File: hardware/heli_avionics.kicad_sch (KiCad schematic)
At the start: 40 parts, among them J1 UPDI, SW1 Reset, U1 ATmega4808-A, U2 nRF24L01P, U3 DRV8212, U4 DRV8212, U5 BMP390L, U6 TPS7A2030PDBV, Y1 16MHz

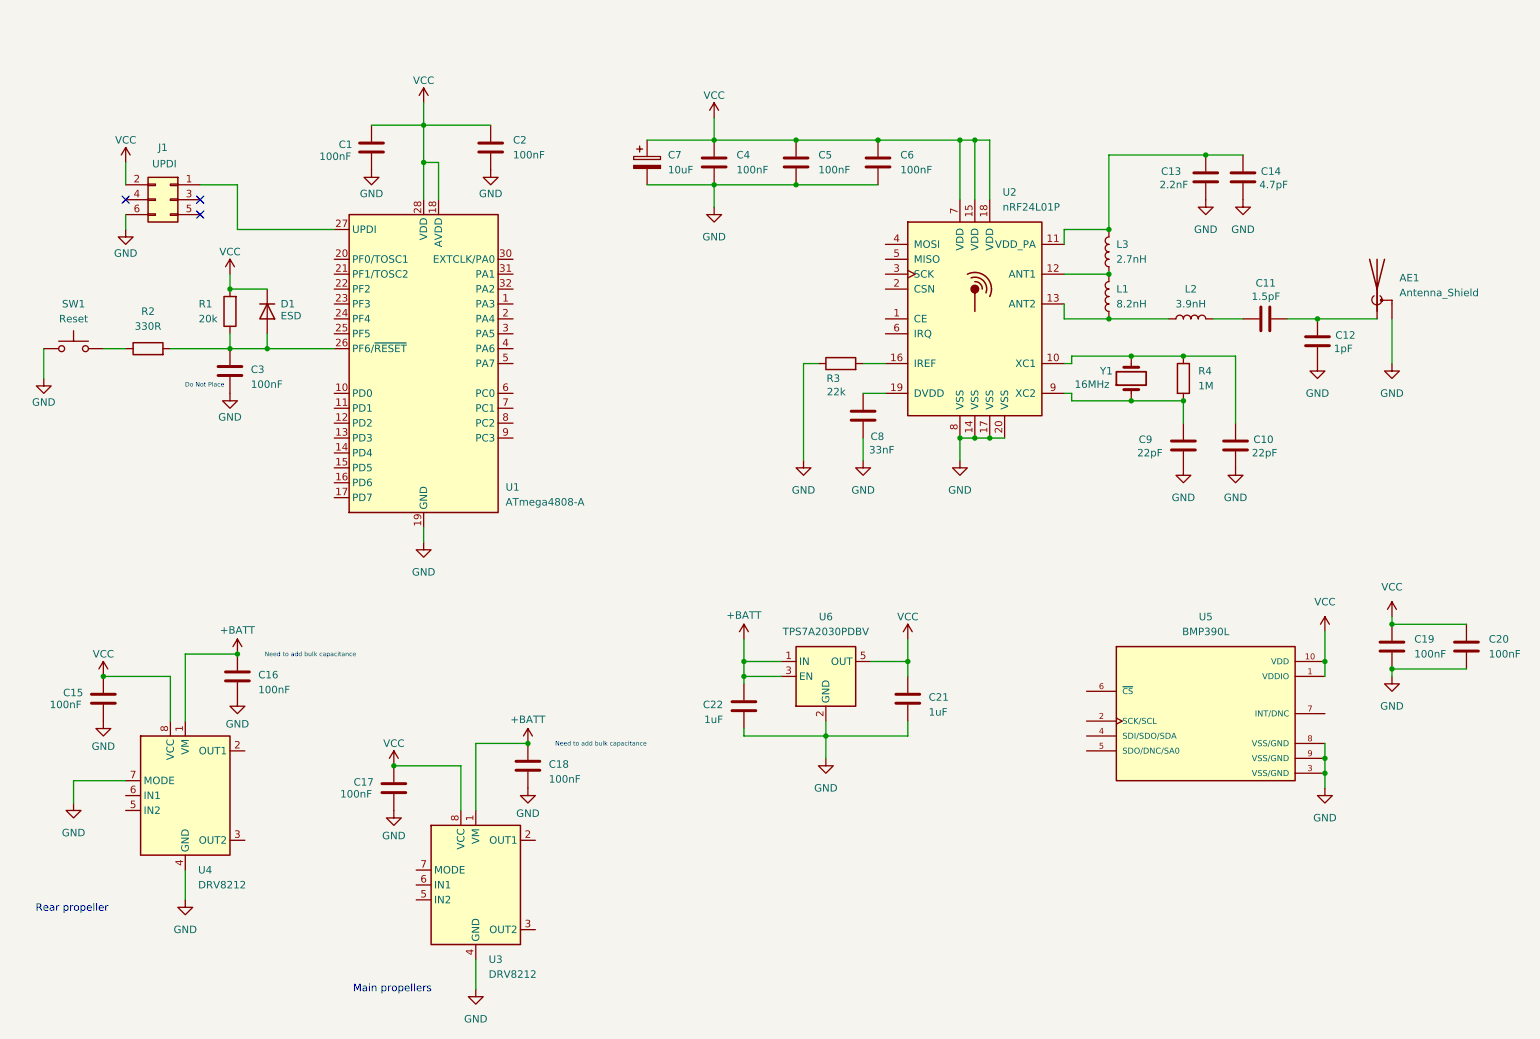
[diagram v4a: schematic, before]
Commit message: Finish motor driver circuits and move to subsheet
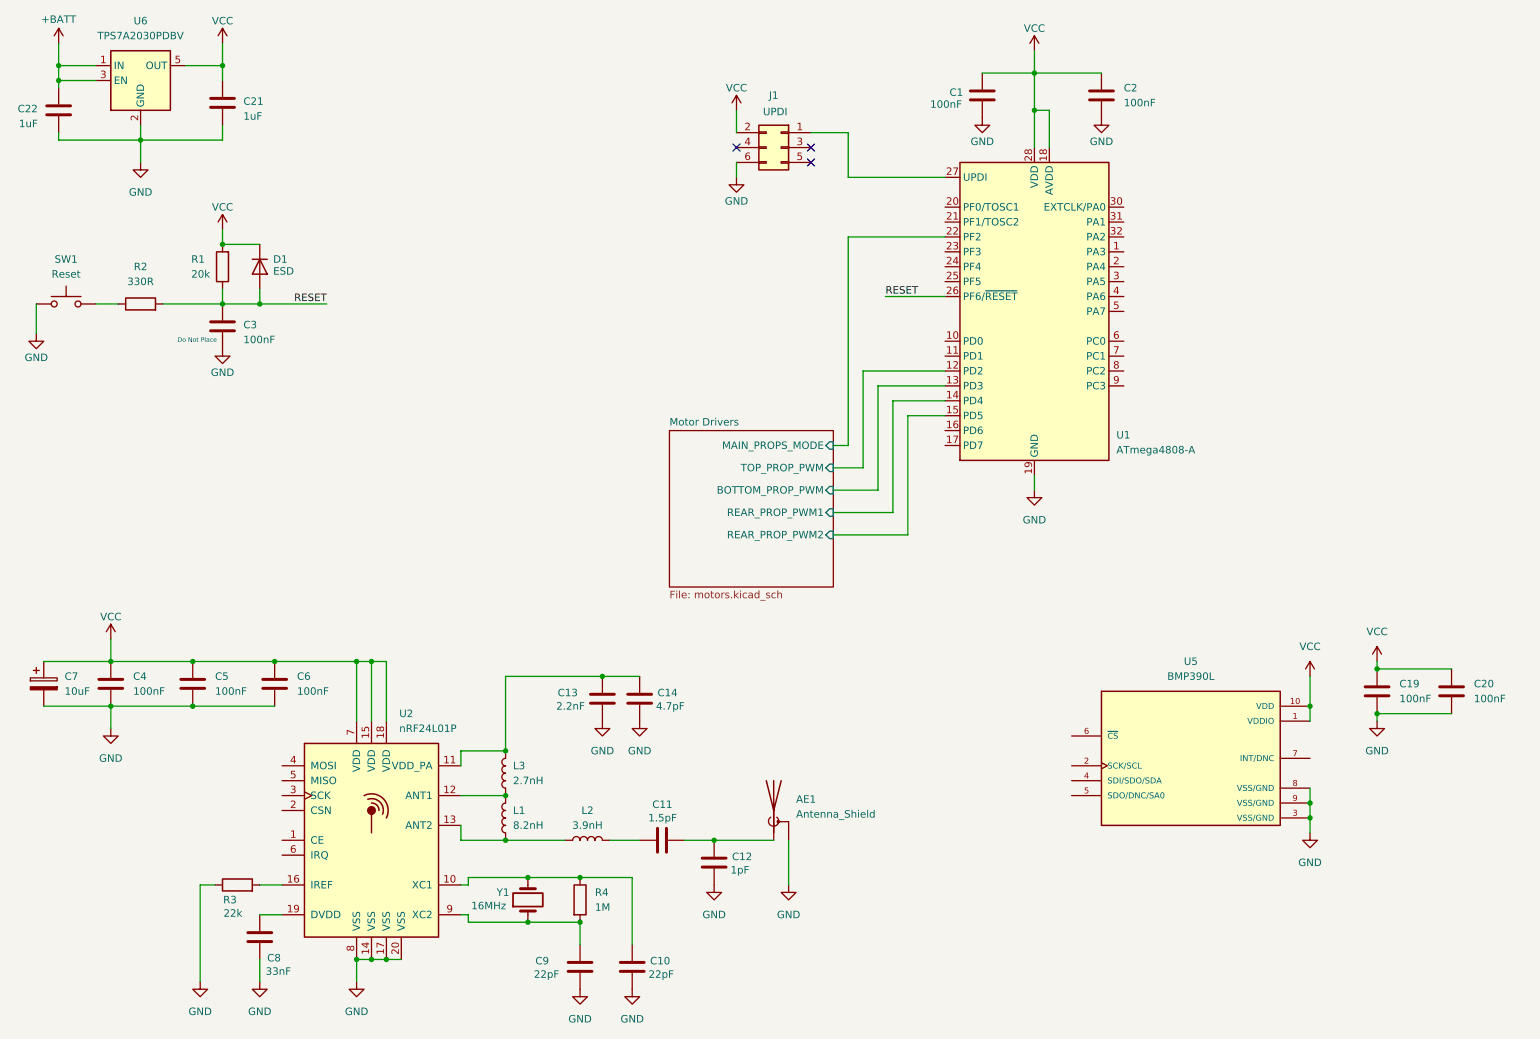
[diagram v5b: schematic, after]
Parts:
- removed C15, C16, C17, C18: 100nF, symbol Device:C
- removed U3, U4: DRV8212, Package_SON:WSON-8-1EP_2x2mm_P0.5mm_EP0.9x1.6mm_ThermalVias, symbol heli_symbols:DRV8212
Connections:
- net RESET: now reaches C3.1, D1.2 (A), R1.1, R2.2, U1.26 (PF6/~{RESET})
- net Motor Drivers/TOP_PROP_PWM: now reaches U1.12 (PD2)
- net Motor Drivers/BOTTOM_PROP_PWM: now reaches U1.13 (PD3)
- net Motor Drivers/REAR_PROP_PWM1: now reaches U1.14 (PD4)
- net Motor Drivers/REAR_PROP_PWM2: now reaches U1.15 (PD5)
- net Motor Drivers/MAIN_PROPS_MODE: now reaches U1.22 (PF2)
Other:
- added sheet Motor Drivers (motors.kicad_sch)
- note removed: "Main propellers"
- note removed: "Need to add bulk capacitance"
- note removed: "Rear propeller"
- moved on the sheet: AE1, C1, C10, C11, C12, C13, C14, C19, C2, C20, C21, C22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

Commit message: Complete pressure sensor circuit
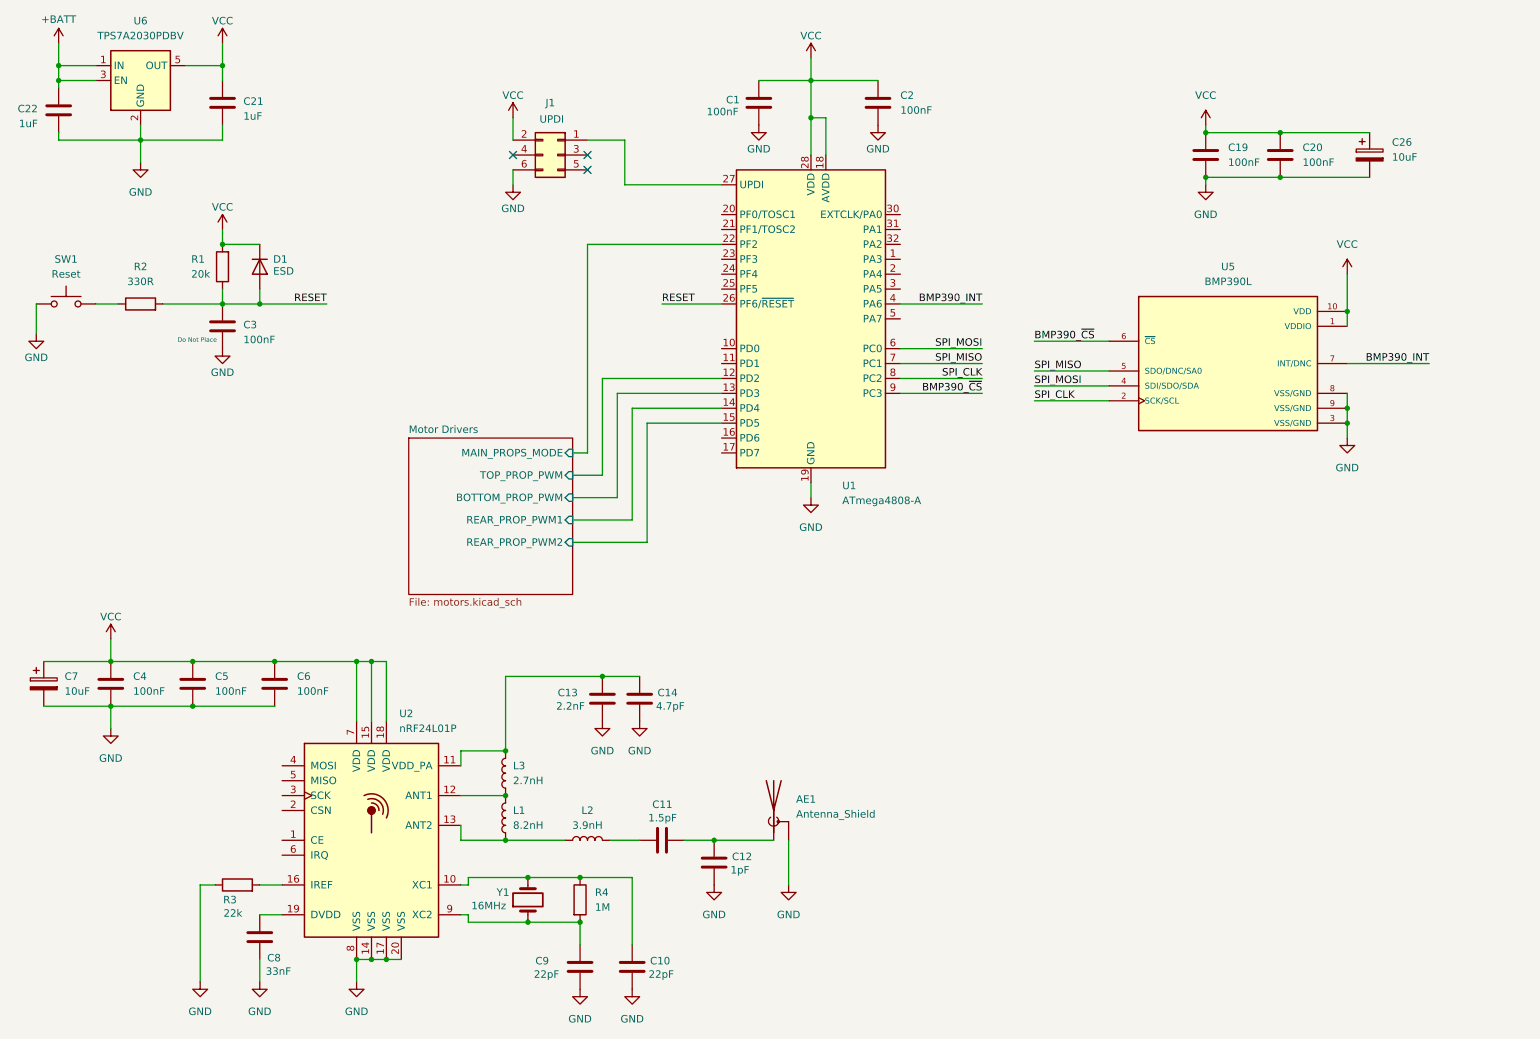
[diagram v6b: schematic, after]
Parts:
- added C26: 10uF, symbol Device:C_Polarized
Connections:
- net GND: now also C26.2
- net VCC: now also C26.1
- net BMP390_INT: now reaches U1.4 (PA6)
- net BMP390_INT: now also U5.7 (INT/DNC)
- net SPI_MOSI: now reaches U1.6 (PC0)
- net SPI_MOSI: now also U5.4 (SDI/SDO/SDA)
- net SPI_MISO: now reaches U1.7 (PC1)
- net SPI_MISO: now also U5.5 (SDO/DNC/SA0)
- net SPI_CLK: now reaches U1.8 (PC2)
- net SPI_CLK: now also U5.2 (SCK/SCL)
- net BMP390_~{CS}: now reaches U1.9 (PC3)
- net BMP390_~{CS}: now also U5.6 (~{CS})
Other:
- moved on the sheet: C1, C19, C2, C20, J1, U1, U5

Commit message: Moved radio circuit to subsheet
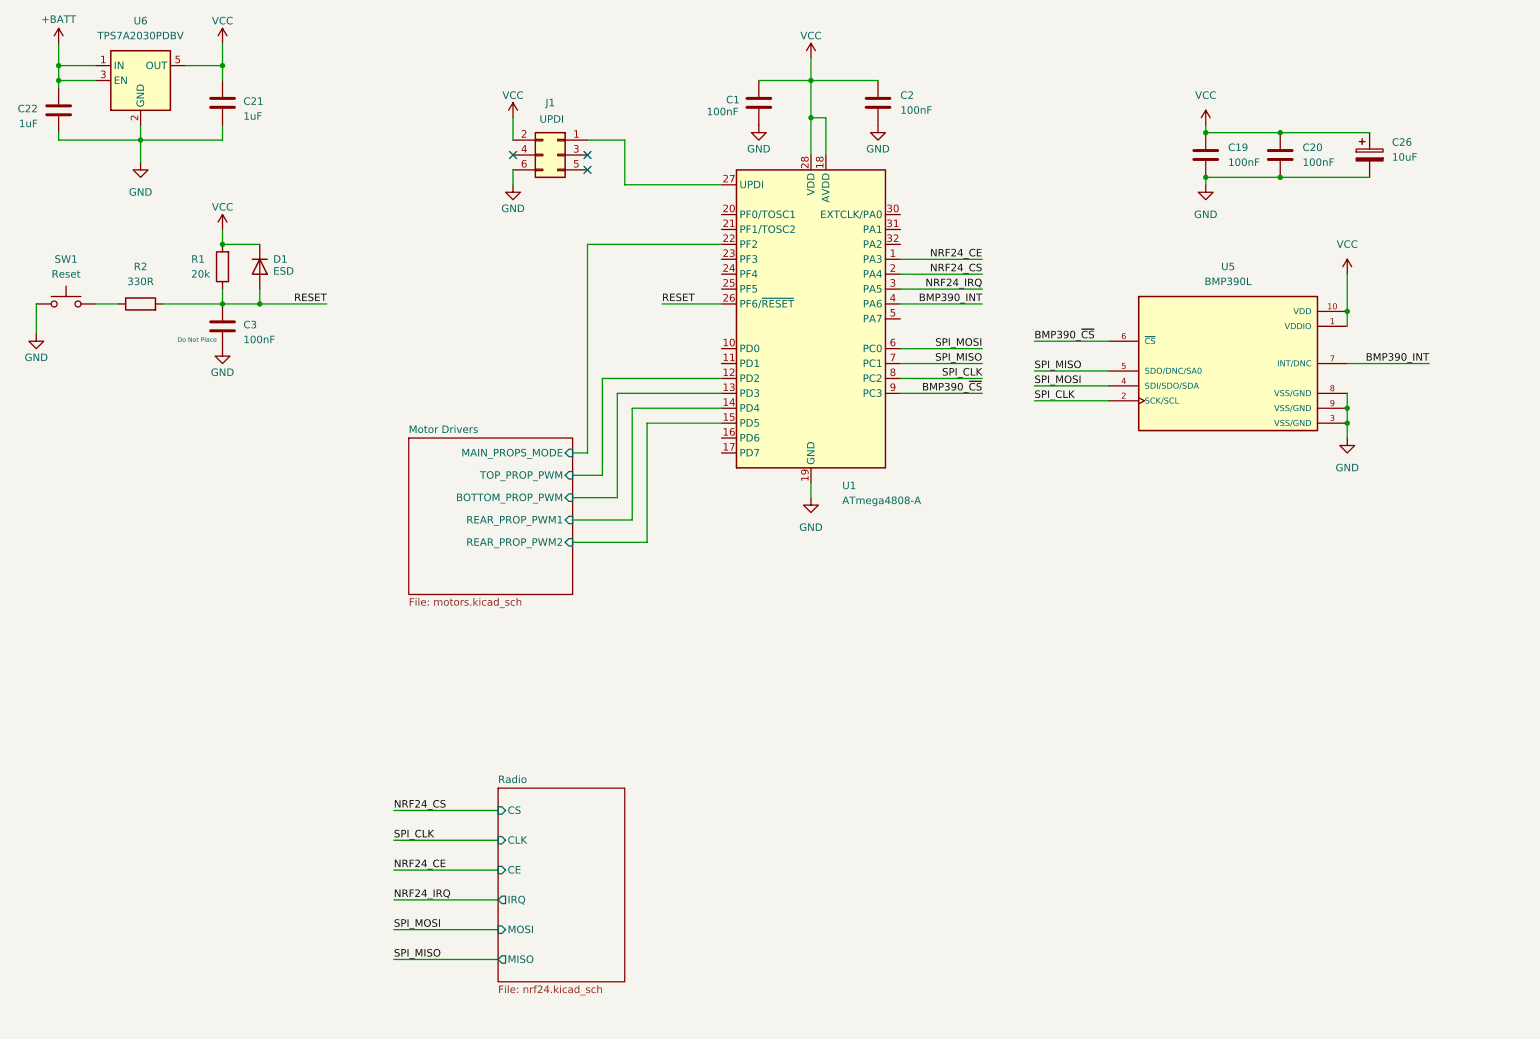
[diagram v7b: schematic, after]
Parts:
- removed AE1: Antenna_Shield, symbol Device:Antenna_Shield
- removed C10, C9: 22pF, symbol Device:C
- removed C11: 1.5pF, symbol Device:C
- removed C12: 1pF, symbol Device:C
- removed C13: 2.2nF, symbol Device:C
- removed C14: 4.7pF, symbol Device:C
- removed C4, C5, C6: 100nF, symbol Device:C
- removed C7: 10uF, symbol Device:C_Polarized
- removed C8: 33nF, symbol Device:C
- removed L1: 8.2nH, symbol Device:L
- removed L2: 3.9nH, symbol Device:L
- removed L3: 2.7nH, symbol Device:L
- removed R3: 22k, symbol Device:R
- removed R4: 1M, symbol Device:R
- removed U2: nRF24L01P, Package_DFN_QFN:QFN-20-1EP_4x4mm_P0.5mm_EP2.5x2.5mm, symbol RF:nRF24L01P
- removed Y1: 16MHz, symbol Device:Crystal
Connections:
- net NRF24_CE: now reaches U1.1 (PA3)
- net NRF24_CS: now reaches U1.2 (PA4)
- net NRF24_IRQ: now reaches U1.3 (PA5)
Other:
- added sheet Radio (nrf24.kicad_sch)

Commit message: Created subsheet for power circuits
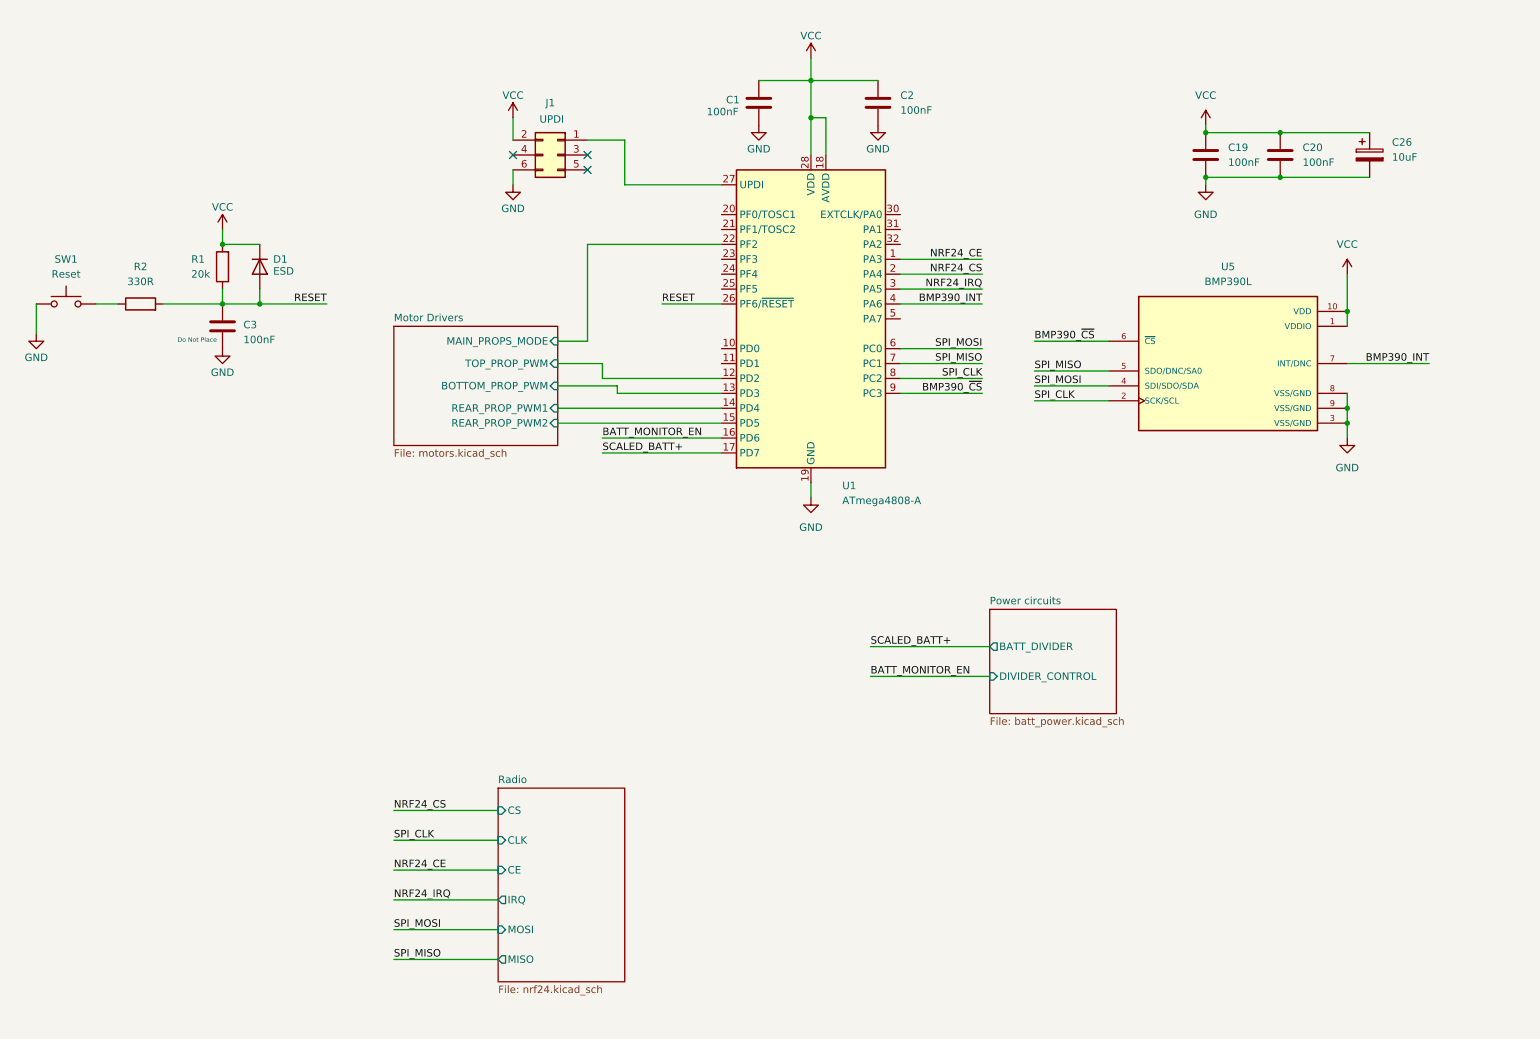
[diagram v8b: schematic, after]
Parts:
- removed C21, C22: 1uF, symbol Device:C
- removed U6: TPS7A2030PDBV, Package_TO_SOT_SMD:SOT-23-5, symbol heli_symbols:TPS7A20
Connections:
- net BATT_MONITOR_EN: now reaches U1.16 (PD6)
- net SCALED_BATT+: now reaches U1.17 (PD7)
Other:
- added sheet Power circuits (batt_power.kicad_sch)
